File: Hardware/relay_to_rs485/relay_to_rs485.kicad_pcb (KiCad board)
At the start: 2 copper layers, 90 x 56 mm, 45 parts, among them J1 Relay Inputs A to E connected, J2 RS485 Output Screw Terminal, J3 INPUT GNDS Screw_Terminal_InputGrounds, J4 Jack-DC, J5 UART OUT, Q1 IRLML6401, U1 ESP32-S3-WROOM-1, U2 MAX485E, U3 SMX1117MP-3.3

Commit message: various edits
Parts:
- added R4: 680R, Resistor_SMD:R_0805_2012Metric_Pad1.20x1.40mm_HandSolder, F.Cu at (160.5, 109.5)
- added R5: 680R, Resistor_SMD:R_0805_2012Metric_Pad1.20x1.40mm_HandSolder, F.Cu at (160.5, 102.0)
- J3: renamed from J3 INPUT GNDS
- TP14: value TP_GND -> ~
- moved G*** 9.86 mm to (134.5, 96.5)
- moved TP16 6.91 mm to (159.5, 82.5)
- moved TP17 1.75 mm to (167.0, 78.0)
- renumbered D1_TVS to D1, TP_B to TP10, TP_RO to TP11, TP_DI to TP12, TP_TX to TP16, TP_RX to TP17, TP_A to TP9
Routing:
- net +3V3: track 113.2 -> 146.7 mm
- net /TX: track 25.4 -> 35.2 mm
- net /B: track 37.9 -> 43.1 mm
- net /A: track 40.4 -> 45.4 mm
- net GND: vias 12 -> 13

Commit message: board updates
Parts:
- TP14: value ~ -> TP_GND

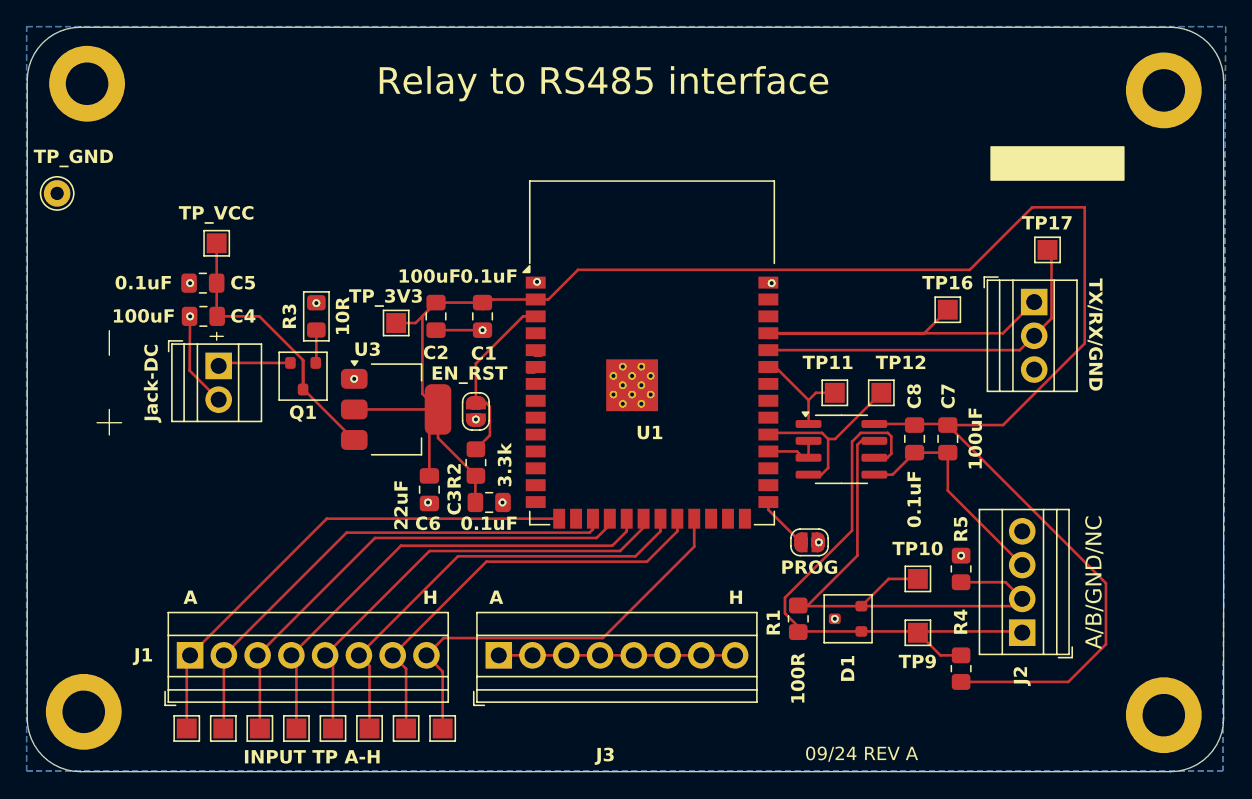
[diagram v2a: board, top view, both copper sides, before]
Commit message: Changed decoupling resistor values from 100uF to 1uF
Too high capacitance
Also changed silkscreen for R1 to make clear terminating resistor
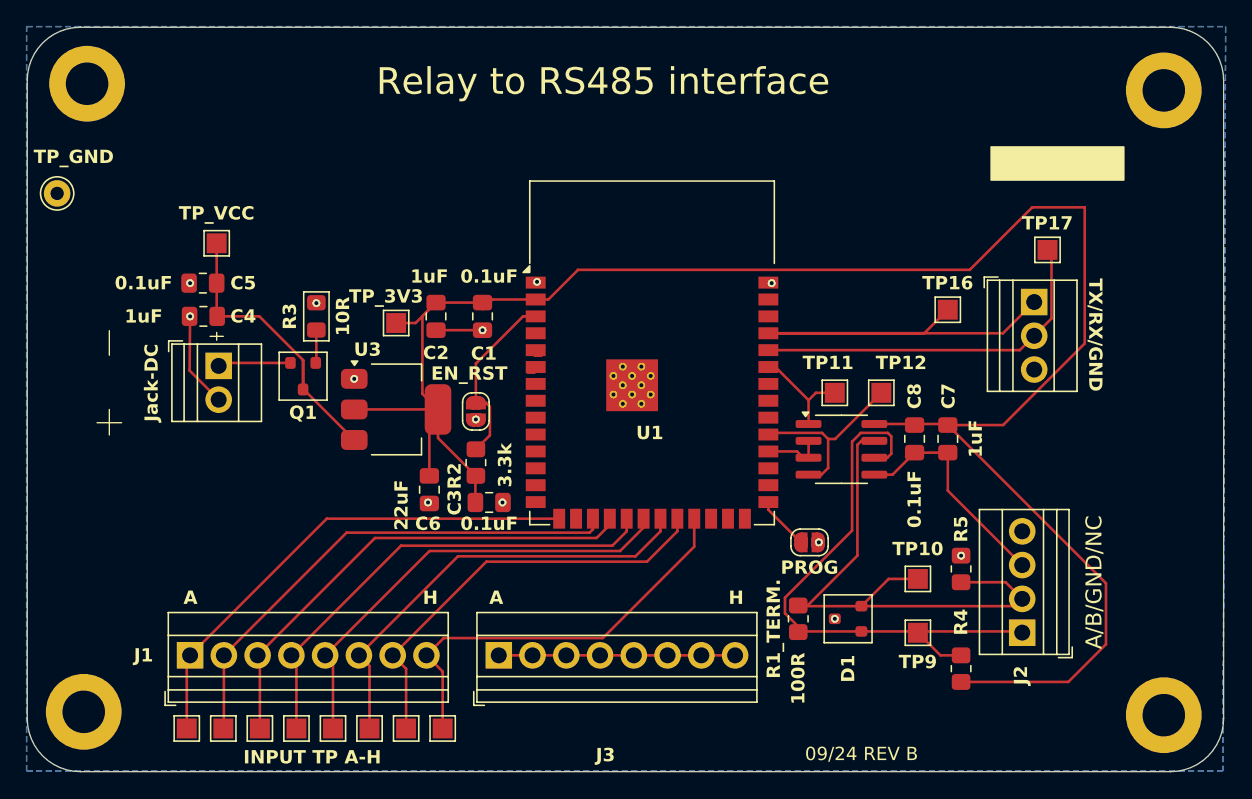
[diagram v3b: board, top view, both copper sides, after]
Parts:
- C2, C4, C7: value 100uF -> 1uF
- renumbered R1 to R1_TERM.
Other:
- board text added: "09/24 REV B"
- board text removed: "09/24 REV A"
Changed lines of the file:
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@@
 			)
 		)
-		(property "Value" "100uF"
+		(property "Value" "1uF"
 			(at -3 0.5 180)
 			(layer "F.SilkS")
@@
 		(descr "Resistor SMD 0805 (2012 Metric), square (rectangular) end terminal, IPC_7351 nominal with elongated pad for handsoldering. (Body size source: IPC-SM-782 page 72, https://www.pcb-3d.com/wordpress/wp-content/uploads/ipc-sm-782a_amendment_1_and_2.pdf), generated with kicad-footprint-generator")
 		(tags "resistor handsolder")
-		(property "Reference" "R1"
-			(at -0.295 -1.8444 90)
+		(property "Reference" "R1_TERM."
+			(at -0.75 -1.8444 90)
 			(layer "F.SilkS")
 			(effects
@@
 			)
 		)
-		(property "Value" "100uF"
+		(property "Value" "1uF"
 			(at 4.5 0 0)
 			(layer "F.SilkS")
@@
 			)
 		)
-		(property "Value" "100uF"
-			(at -0.0125 -2.1 -90)
+		(property "Value" "1uF"
+			(at -0.0125 -2.1 270)
 			(layer "F.SilkS")
 			(effects
@@
 		)
 	)
-	(gr_text "09/24 REV A"
+	(gr_text "09/24 REV B"
 		(at 148.75 116.5 0)
 		(layer "F.SilkS")

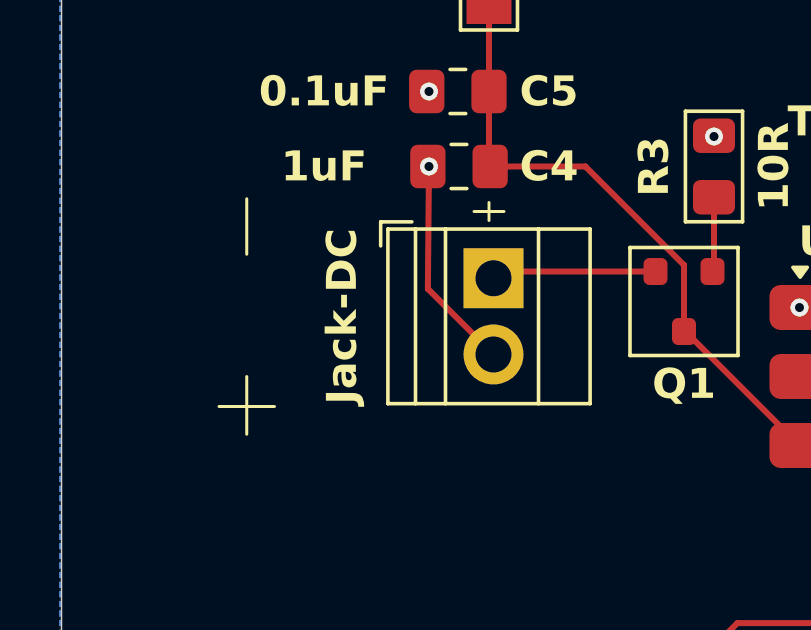
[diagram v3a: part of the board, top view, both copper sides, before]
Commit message: Change of DC polarity marking on PCB
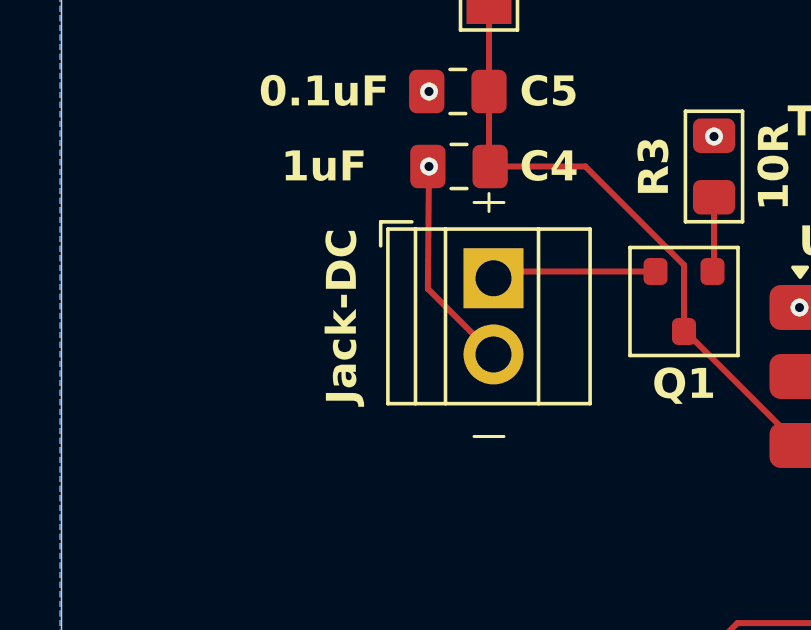
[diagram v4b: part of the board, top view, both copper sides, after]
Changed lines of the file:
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@@
 		)
 		(property "Value" "1uF"
-			(at -0.0125 -2.1 270)
+			(at -0.0125 -2.1 -90)
 			(layer "F.SilkS")
 			(effects
@@
 	)
 	(gr_line
-		(start 95.5 91)
-		(end 97.35 91)
+		(start 104 84.2)
+		(end 105 84.2)
 		(stroke
 			(width 0.1)
@@
 	)
 	(gr_line
-		(start 104 84.5)
-		(end 105 84.5)
-		(stroke
-			(width 0.1)
-			(type default)
-		)
-		(layer "F.SilkS")
-	)
-	(gr_line
-		(start 96.425 90)
-		(end 96.425 91.925)
+		(start 104 92)
+		(end 105 92)
 		(stroke
 			(width 0.1)
@@
 	)
 	(gr_line
-		(start 104.5 84.2)
-		(end 104.5 84.8)
+		(start 104.5 83.9)
+		(end 104.5 84.5)
 		(stroke
 			(width 0.1)
-			(type default)
-		)
-		(layer "F.SilkS")
-	)
-	(gr_line
-		(start 96.425 85.925)
-		(end 96.425 84.075)
-		(stroke
-			(width 0.1)

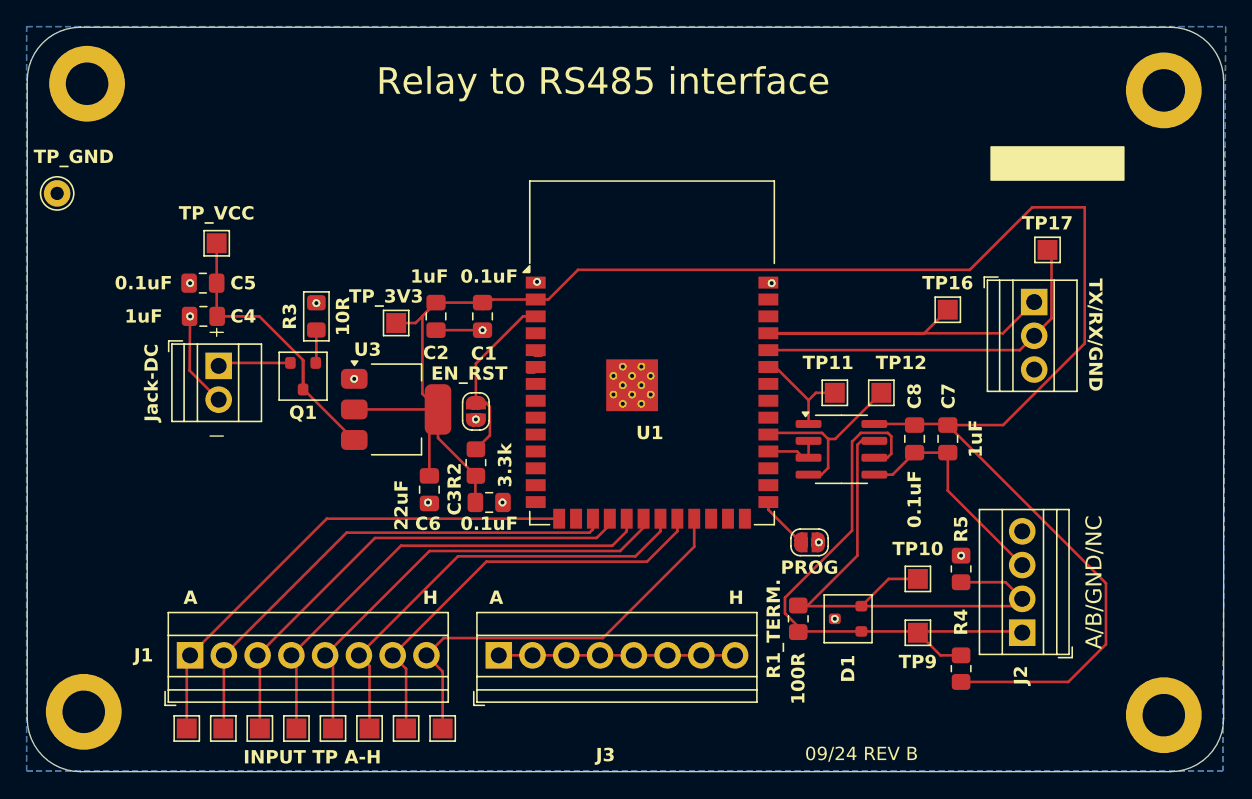
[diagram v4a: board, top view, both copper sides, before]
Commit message: Revision B of Board (2.0.0)
Add:
1. LC filter on 3.3V input
2. Change trace widths to 20mil for 3.3V and 25mil for VCC as per Espressif documentation
3. Add-in 470R UART Tx resistors to suppress 80MHz harmonics
4. Rerouting of components around MAX3485 chip
5. Change value of R2 EN pullup resistor to 4.7k
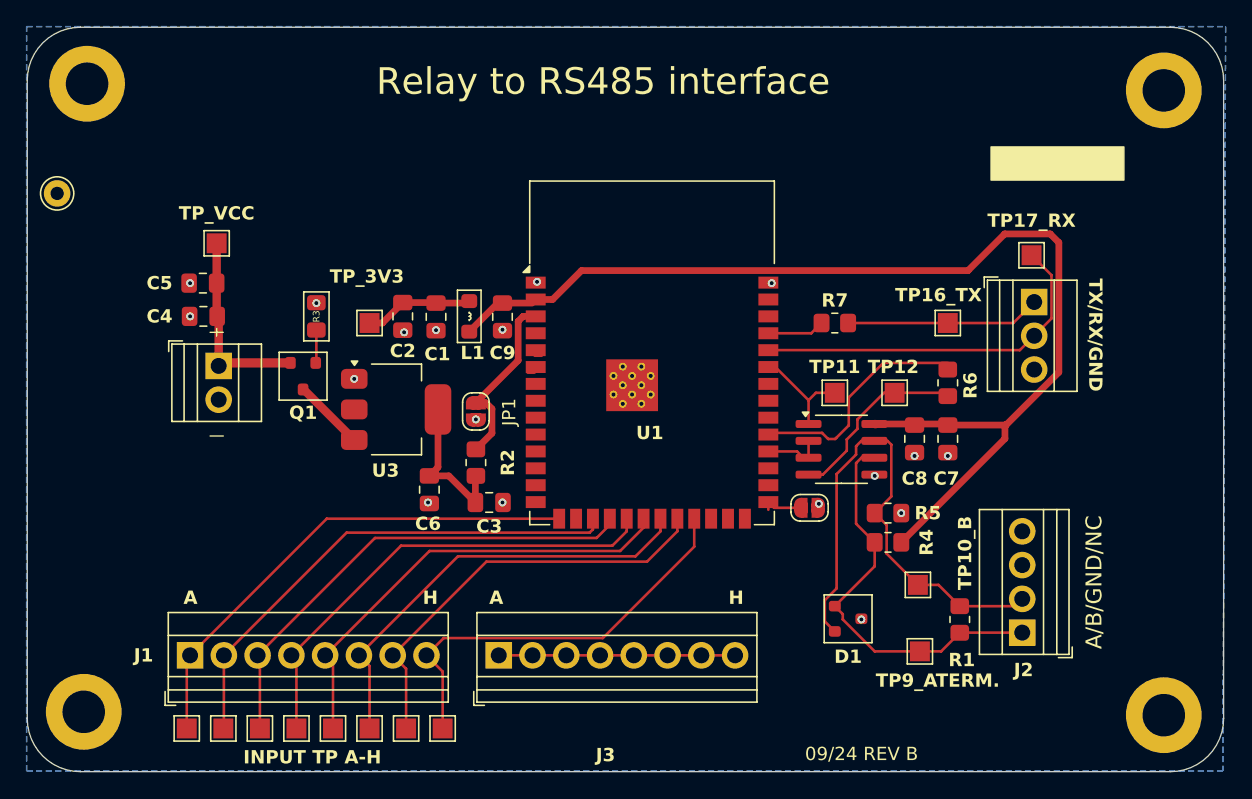
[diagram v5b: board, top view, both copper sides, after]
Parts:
- added C9: 0.1uF, Capacitor_SMD:C_0805_2012Metric_Pad1.18x1.45mm_HandSolder, F.Cu at (126.0, 83.0)
- added L1: 2.2nH, PCM_Inductor_SMD_AKL:L_0805_2012Metric_Pad1.05x1.20mm_HandSolder, F.Cu at (123.5, 83.0)
- added R6: 470R, Resistor_SMD:R_0805_2012Metric_Pad1.20x1.40mm_HandSolder, F.Cu at (159.5, 88.0)
- added R7: 470R, Resistor_SMD:R_0805_2012Metric_Pad1.20x1.40mm_HandSolder, F.Cu at (151.0, 83.5)
- R2: value 3.3k -> 4.7k
- moved R1 12.2 mm to (160.4, 105.8)
- moved R4 11.0 mm to (155.0, 100.0), turned to 180 degrees
- moved R5 6.92 mm to (155.0, 97.8), turned to 0 degrees
- moved C1 3.50 mm to (121.0, 83.0)
- moved JP2 2.60 mm to (149.1, 97.4)
- moved C2 2.50 mm to (118.5, 83.0)
- moved TP13 2.00 mm to (116.0, 83.5)
- moved TP9_A 1.41 mm to (157.4, 108.2)
- moved TP17_RX 1.26 mm to (165.8, 78.4)
- moved TP12 1.00 mm to (155.5, 88.8)
- moved TP16_TX 1.00 mm to (159.5, 83.5)
- moved TP10_B 0.45 mm to (157.2, 103.2)
- turned D1 to 0 degrees
- renumbered R1_TERM. to R1, TP10 to TP10_B, TP16 to TP16_TX, TP17 to TP17_RX, TP9 to TP9_A
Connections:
- J4 pad 1: Net-(Q1-S) -> VCC
- Q1 pad 2: Net-(Q1-S) -> VCC
- TP12 pad 1: Net-(U1-IO38) -> Net-(U2-DI)
- U1 pad 37: /TX -> Net-(U1-TXD0)
- U2 pad 4: Net-(U1-IO38) -> Net-(U2-DI)
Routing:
- net +3V3: track 146.7 -> 105.7 mm
- net GND: track 45.5 -> 17.9 mm, vias 13 -> 18
- net /TX: track 35.2 -> 14.7 mm
- net Net-(U2-DI): track 0.00 -> 14.4 mm
- net /A: track 45.4 -> 31.9 mm
- net Net-(Q1-S): track 5.49 -> 0.00 mm
- net Net-(U1-TXD0): track 0.00 -> 4.32 mm
- net /B: track 43.1 -> 39.3 mm
- net Net-(U1-IO38): track 14.0 -> 17.3 mm
- net VCC: track 23.2 -> 20.2 mm
- net Net-(JP2-A): track 4.04 -> 3.21 mm
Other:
- board text added: "TERM."

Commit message: Minor change
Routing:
- net +3V3: track 105.7 -> 114.4 mm
- net GND: vias 18 -> 19
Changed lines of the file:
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@@
 		(tags "resistor handsolder")
 		(property "Reference" "R6"
-			(at -0.2 1.7 270)
+			(at -0.2 1.7 -90)
 			(layer "F.SilkS")
 			(effects
@@
 		(tags "SOT-23")
 		(property "Reference" "D1"
-			(at 0 2.85 360)
+			(at 0 2.85 0)
 			(layer "F.SilkS")
 			(effects
@@
 		)
 		(property "Value" "SM712 TVS"
-			(at 0 2.5 360)
+			(at 0 2.5 0)
 			(layer "F.Fab")
 			(hide yes)
@@
 		)
 		(property "Footprint" "PCM_Package_TO_SOT_SMD_AKL:SOT-23"
-			(at 0 0 360)
+			(at 0 0 0)
 			(layer "F.Fab")
 			(hide yes)
@@
 		)
 		(property "Datasheet" "https://www.tme.eu/Document/75933fc1842e5f5f3391c0542bf992c7/SM712.pdf"
-			(at 0 0 360)
+			(at 0 0 0)
 			(layer "F.Fab")
 			(hide yes)
@@
 		)
 		(property "Description" "SOT-23 Dual bidirectional TVS diode, 12V/7V, 600W, Alternate KiCAD Library"
-			(at 0 0 360)
+			(at 0 0 0)
 			(layer "F.Fab")
 			(hide yes)
@@
 		(tags "capacitor handsolder")
 		(property "Reference" "C1"
-			(at 2.8 -0.1 360)
+			(at 2.8 -0.1 0)
 			(layer "F.SilkS")
 			(effects
@@
 		)
 		(property "Value" "0.1uF"
-			(at -3 0.5 360)
+			(at -3 0.5 0)
 			(layer "F.SilkS")
 			(hide yes)
@@
 		)
 		(fp_text user "${REFERENCE}"
-			(at 0 0 360)
+			(at 0 0 0)
 			(layer "F.Fab")
 			(effects
@@
 		)
 		(property "Value" "680R"
-			(at 0 1.65 360)
+			(at 0 1.65 0)
 			(layer "F.Fab")
 			(hide yes)
@@
 		)
 		(property "Value" "2.2nH"
-			(at 3 2 360)
+			(at 3 2 0)
 			(layer "F.Fab")
 			(hide yes)
@@
 		(tags "resistor handsolder")
 		(property "Reference" "R5"
-			(at 3 0 360)
+			(at 3 0 0)
 			(layer "F.SilkS")
 			(effects
@@
 		)
 		(property "Value" "680R"
-			(at 0 1.65 360)
+			(at 0 1.65 0)
 			(layer "F.Fab")
 			(hide yes)
@@
 		)
 		(fp_text user "${REFERENCE}"
-			(at 0 0 360)
+			(at 0 0 0)
 			(layer "F.Fab")
 			(effects
@@
 	)
 	(via
-		(at 114.85 87.701)
+		(at 115.4 87.701)
 		(size 0.6)
 		(drill 0.3)
@@
 	)
 	(via
+		(at 114.4 87.8)
+		(size 0.6)
+		(drill 0.3)
+		(layers "F.Cu" "B.Cu")
+		(teardrops
+			(best_length_ratio 0.5)
+			(max_length 1)
+			(best_width_ratio 1)
+			(max_width 2)
+			(curve_points 0)
+			(filter_ratio 0.9)
+			(enabled yes)
+			(allow_two_segments yes)
+			(prefer_zone_connections yes)
+		)
+		(net 1)
+	)
+	(via
 		(at 102.5 83)
 		(size 0.6)
@@
 	)
 	(segment
+		(start 121.15 90)
+		(end 116 84.85)
+		(width 0.508)
+		(layer "F.Cu")
+		(net 2)
+	)
+	(segment
 		(start 131.944 79.556)
 		(end 129.77 81.73)
@@
 	)
 	(segment
+		(start 116 84.85)
+		(end 116 83.5)
+		(width 0.508)
+		(layer "F.Cu")
+		(net 2)
+	)
+	(segment
 		(start 121 82)
 		(end 123.35 82)
@@
 	)
 	(zone
+		(net 2)
+		(net_name "+3V3")
+		(layer "F.Cu")
+		(name "$teardrop_padvia$")
+		(hatch full 0.1)
+		(priority 30000)
+		(attr
+			(teardrop
+				(type padvia)
+			)
+		)
+		(connect_pads yes
+			(clearance 0)
+		)
+		(min_thickness 0.0254)
+		(filled_areas_thickness no)
+		(fill yes
+			(thermal_gap 0.5)
+			(thermal_bridge_width 0.5)
+			(island_removal_mode 1)
+			(island_area_min 10)
+		)
+		(polygon
+			(pts
+				(xy 119.622499 88.113289) (xy 119.263289 88.472499) (xy 120.15 90.414214) (xy 121.150707 90.000707)
+				(xy 120.65 88.1)
+			)
+		)
+	)
+	(zone
 		(net 8)
 		(net_name "/InputB")
@@
 			)
 		)
+	)
+	(zone
+		(net 2)
+		(net_name "+3V3")
+		(layer "F.Cu")
+		(name "$teardrop_padvia$")
+		(hatch full 0.1)
+		(priority 30001)
+		(attr
+			(teardrop
+				(type padvia)
+			)
+		)
+		(connect_pads yes
+			(clearance 0)
+		)
+		(min_thickness 0.0254)
+		(filled_areas_thickness no)
+		(fill yes
+			(thermal_gap 0.5)
+			(thermal_bridge_width 0.5)
+			(island_removal_mode 1)
+			(island_area_min 10)
+		)
+		(polygon
+			(pts
+				(xy 115.926461 85.135671) (xy 116.285671 84.776461) (xy 116.75 84.25) (xy 115.999293 83.499293)
+				(xy 115.302303 84.25)
+			)
+		)

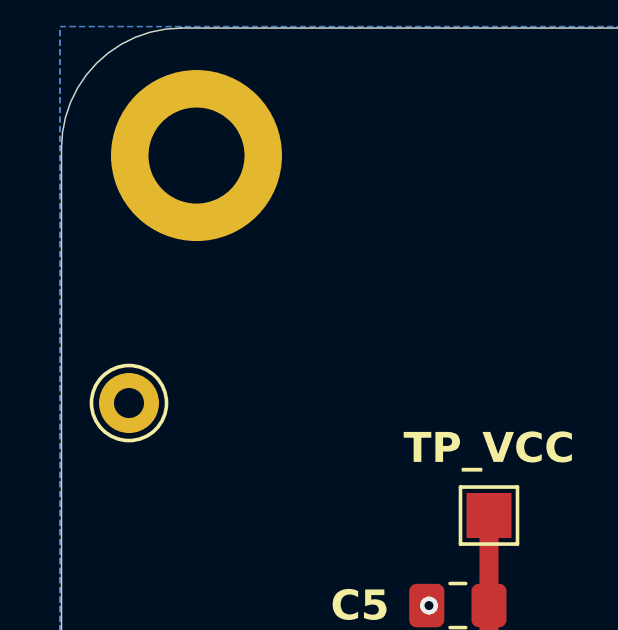
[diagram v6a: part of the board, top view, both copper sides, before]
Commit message: Forgot TP_GND
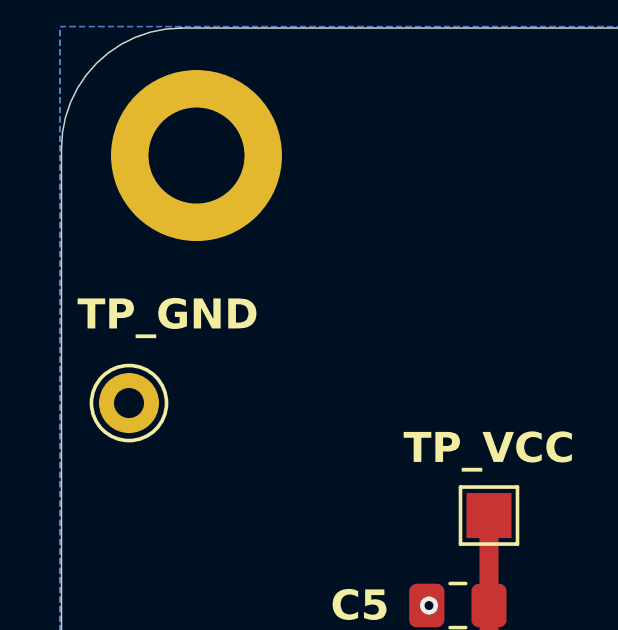
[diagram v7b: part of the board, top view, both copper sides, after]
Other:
- board text added: "TP_GND"
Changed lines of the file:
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@@
+		)
+	)
+	(gr_text "TP_GND"
+		(at 93.8 70.8 0)
+		(layer "F.SilkS")
+		(effects
+			(font
+				(size 1 1)
+				(thickness 0.2)
+				(bold yes)
+			)
 		)
 	)
@@
 			)
 		)
-	)
-	(gr_text "${REFERENCE}"
-		(at 92.5 76 0)
-		(layer "F.Fab")
-		(effects
-			(font
-				(size 1 1)
-				(thickness 0.15)
-			)
-		)

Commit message: Fiddling around with TP_GND position
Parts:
- moved TP14 1.67 mm to (93.8, 74.8)
